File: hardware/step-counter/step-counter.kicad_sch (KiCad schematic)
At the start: 50 parts, among them J1 Conn_01x10_Male, J2 Conn_01x14_Male, J3 Conn_01x10_Male, J4 Conn_Power, U1 74HC161, U10 74HC161, U11 74LVC1G02, U12 74LVC2G04, U13 74HC4024, U14 74LVC1G332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

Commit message: Updated PCBs
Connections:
- net Q0: now also J2.13 (Pin_13); no longer J2.8 (Pin_8)
- net Q1: now also J2.12 (Pin_12); no longer J2.9 (Pin_9)
- net Q2: now also J2.11 (Pin_11); no longer J2.10 (Pin_10)
- net Q3: now also J2.10 (Pin_10); no longer J2.11 (Pin_11)
- net Q4: now also J2.9 (Pin_9); no longer J2.12 (Pin_12)
- net Q5: now also J2.8 (Pin_8); no longer J2.13 (Pin_13)
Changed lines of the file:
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@@
     (effects (font (size 1.27 1.27)) (justify left bottom))
   )
-  (label "Q1" (at 393.7 153.67 0)
+  (label "Q1" (at 393.7 161.29 0)
     (effects (font (size 1.27 1.27)) (justify left bottom))
   )
@@
     (effects (font (size 1.27 1.27)) (justify right bottom))
   )
-  (label "Q0" (at 393.7 151.13 0)
+  (label "Q0" (at 393.7 163.83 0)
     (effects (font (size 1.27 1.27)) (justify left bottom))
   )
-  (label "Q3" (at 393.7 158.75 0)
+  (label "Q3" (at 393.7 156.21 0)
     (effects (font (size 1.27 1.27)) (justify left bottom))
   )
@@
     (effects (font (size 1.27 1.27)) (justify right bottom))
   )
-  (label "Q5" (at 393.7 163.83 0)
+  (label "Q5" (at 393.7 151.13 0)
     (effects (font (size 1.27 1.27)) (justify left bottom))
   )
-  (label "Q2" (at 393.7 156.21 0)
+  (label "Q2" (at 393.7 158.75 0)
     (effects (font (size 1.27 1.27)) (justify left bottom))
   )
@@
     (effects (font (size 1.27 1.27)) (justify left bottom))
   )
-  (label "Q4" (at 393.7 161.29 0)
+  (label "Q4" (at 393.7 153.67 0)
     (effects (font (size 1.27 1.27)) (justify left bottom))
   )

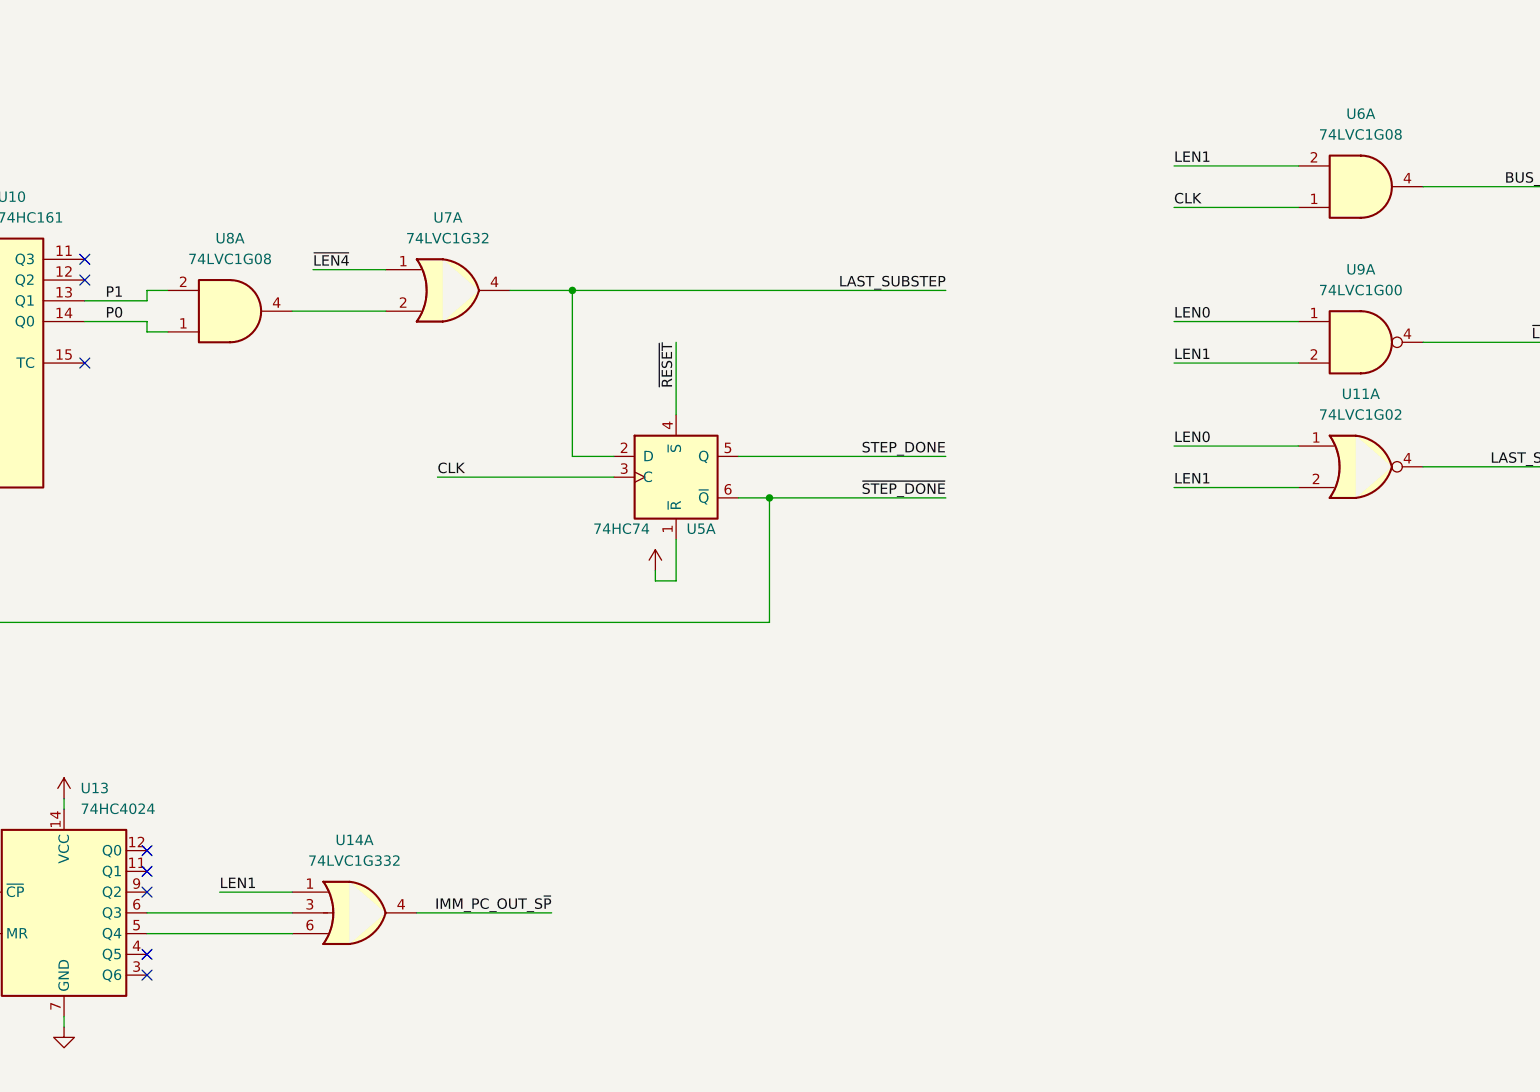
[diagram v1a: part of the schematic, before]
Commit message: Updated opcode and step counter PCBs
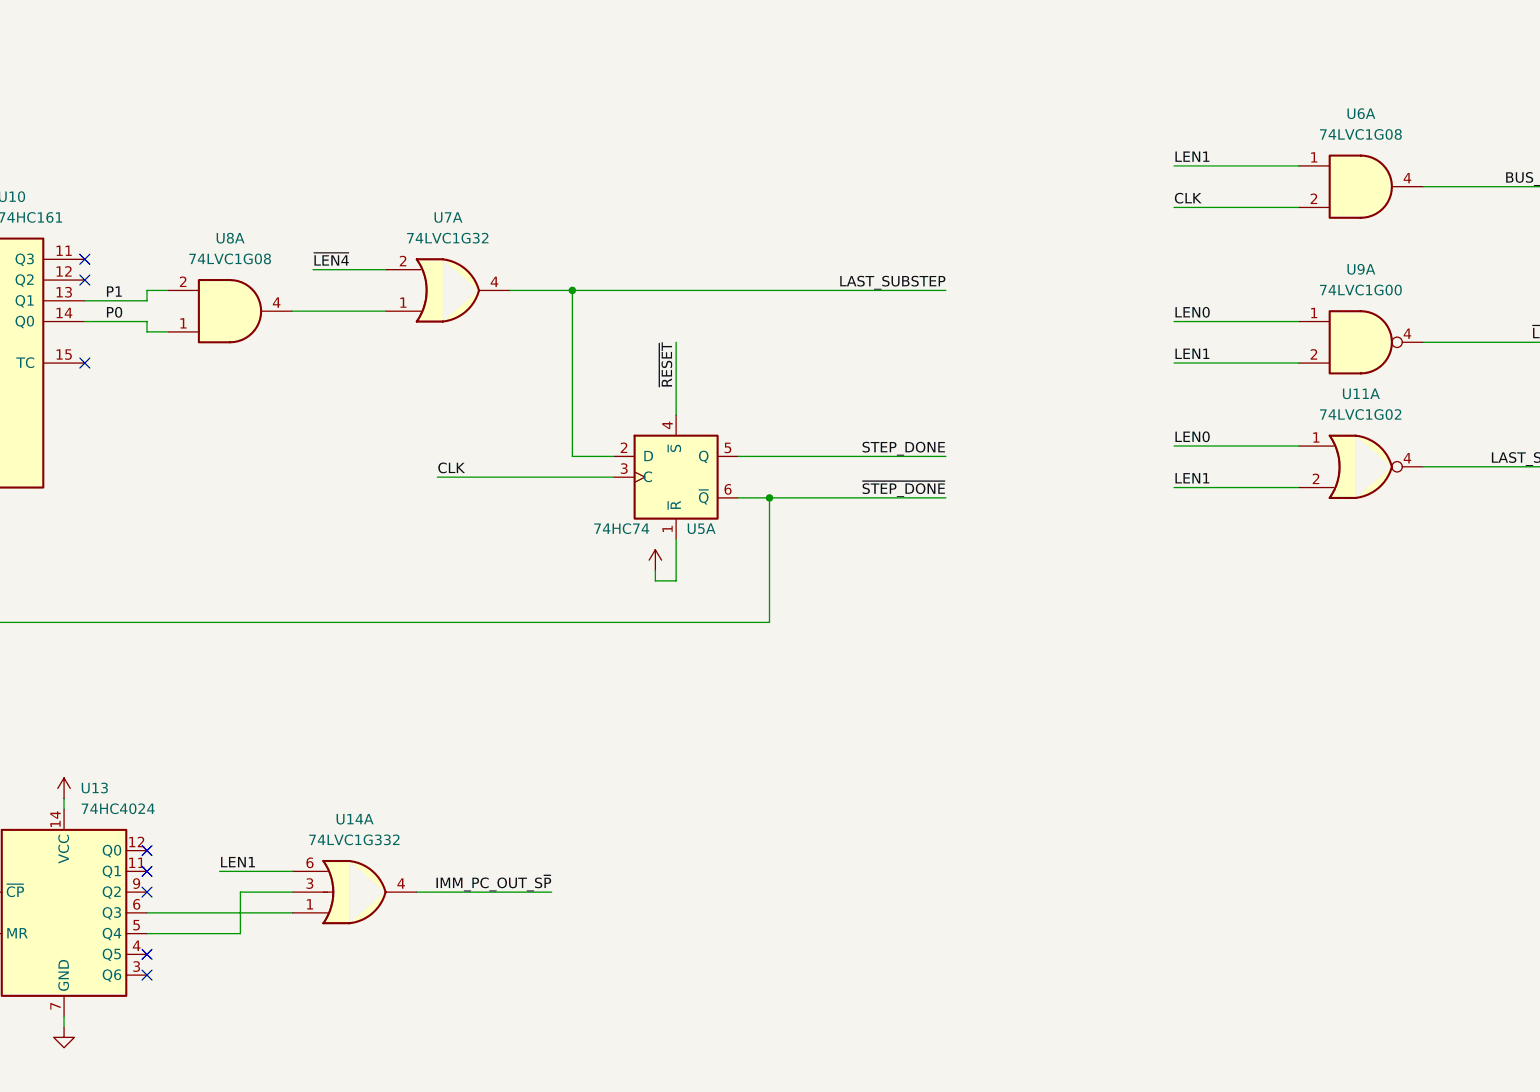
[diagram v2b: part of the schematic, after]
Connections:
- net CLK: now also U6.2; no longer U6.1
- net LEN1: now also U14.6, U6.1; no longer U14.1, U6.2
- net ~{LEN4}: now also U7.2; no longer U7.1
- net at U13.5 (Q4): now also U14.3; no longer U14.6
- net at U13.6 (Q3): now also U14.1; no longer U14.3
- net at U8.4: now also U7.1; no longer U7.2
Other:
- moved on the sheet: U14A
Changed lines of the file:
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@@
+    (stroke (width 0) (type default) (color 0 0 0 0))
+  )
+  (wire (pts (xy 96.52 246.38) (xy 114.3 246.38))
     (stroke (width 0) (type default) (color 0 0 0 0))
   )
@@
     (stroke (width 0) (type default) (color 0 0 0 0))
   )
-  (wire (pts (xy 96.52 246.38) (xy 114.3 246.38))
-    (stroke (width 0) (type default) (color 0 0 0 0))
-  )
   (wire (pts (xy 140.97 97.79) (xy 144.78 97.79))
     (stroke (width 0) (type default) (color 0 0 0 0))
@@
     (stroke (width 0) (type default) (color 0 0 0 0))
   )
-  (wire (pts (xy 129.54 246.38) (xy 146.05 246.38))
+  (wire (pts (xy 129.54 243.84) (xy 146.05 243.84))
     (stroke (width 0) (type default) (color 0 0 0 0))
   )
@@
     (stroke (width 0) (type default) (color 0 0 0 0))
   )
-  (wire (pts (xy 105.41 243.84) (xy 114.3 243.84))
+  (wire (pts (xy 105.41 241.3) (xy 114.3 241.3))
     (stroke (width 0) (type default) (color 0 0 0 0))
   )
@@
     (stroke (width 0) (type default) (color 0 0 0 0))
   )
+  (wire (pts (xy 107.95 243.84) (xy 114.3 243.84))
+    (stroke (width 0) (type default) (color 0 0 0 0))
+  )
   (wire (pts (xy 66.04 309.88) (xy 76.2 309.88))
     (stroke (width 0) (type default) (color 0 0 0 0))
@@
     (stroke (width 0) (type default) (color 0 0 0 0))
   )
+  (wire (pts (xy 107.95 248.92) (xy 107.95 243.84))
+    (stroke (width 0) (type default) (color 0 0 0 0))
+  )
   (wire (pts (xy 140.97 87.63) (xy 156.21 87.63))
     (stroke (width 0) (type default) (color 0 0 0 0))
@@
     (stroke (width 0) (type default) (color 0 0 0 0))
   )
-  (wire (pts (xy 96.52 248.92) (xy 114.3 248.92))
-    (stroke (width 0) (type default) (color 0 0 0 0))
-  )
   (wire (pts (xy 55.88 179.07) (xy 55.88 210.82))
+    (stroke (width 0) (type default) (color 0 0 0 0))
+  )
+  (wire (pts (xy 96.52 248.92) (xy 107.95 248.92))
     (stroke (width 0) (type default) (color 0 0 0 0))
   )
@@
     (effects (font (size 1.27 1.27)) (justify left bottom))
   )
-  (label "IMM_PC_OUT_S~{P}" (at 146.05 246.38 180)
+  (label "IMM_PC_OUT_S~{P}" (at 146.05 243.84 180)
     (effects (font (size 1.27 1.27)) (justify right bottom))
   )
@@
     (effects (font (size 1.27 1.27)) (justify left bottom))
   )
-  (label "LEN1" (at 105.41 243.84 0)
+  (label "LEN1" (at 105.41 241.3 0)
     (effects (font (size 1.27 1.27)) (justify left bottom))
   )
@@
     (pin "4")
   )
-  (symbol (lib_id "riscv-serial:74LVC1G332") (at 121.92 246.38 0) (unit 1)
-    (in_bom yes) (on_board yes) (fields_autoplaced)
-    (property "Reference" "U14" (id 0) (at 121.92 237.49 0))
-    (property "Value" "74LVC1G332" (id 1) (at 121.92 240.03 0))
-    (property "Footprint" "Package_TO_SOT_SMD:SOT-23-6_Handsoldering" (id 2) (at 121.158 247.142 0)
-      (effects (font (size 1.27 1.27)) hide)
-    )
-    (property "Datasheet" "" (id 3) (at 121.158 247.142 0)
+  (symbol (lib_id "riscv-serial:74LVC1G332") (at 121.92 243.84 0) (mirror x) (unit 1)
+    (in_bom yes) (on_board yes) (fields_autoplaced)
+    (property "Reference" "U14" (id 0) (at 121.92 234.95 0))
+    (property "Value" "74LVC1G332" (id 1) (at 121.92 237.49 0))
+    (property "Footprint" "Package_TO_SOT_SMD:SOT-23-6_Handsoldering" (id 2) (at 121.158 243.078 0)
+      (effects (font (size 1.27 1.27)) hide)
+    )
+    (property "Datasheet" "" (id 3) (at 121.158 243.078 0)
       (effects (font (size 1.27 1.27)) hide)
     )
@@
     (pin "1")
   )
-  (symbol (lib_id "riscv-serial:74LVC1G08") (at 245.11 157.48 0) (mirror x) (unit 1)
+  (symbol (lib_id "riscv-serial:74LVC1G08") (at 245.11 157.48 0) (unit 1)
     (in_bom yes) (on_board yes) (fields_autoplaced)
     (property "Reference" "U6" (id 0) (at 245.11 148.59 0))
     (property "Value" "74LVC1G08" (id 1) (at 245.11 151.13 0))
-    (property "Footprint" "Package_TO_SOT_SMD:SOT-23-5_HandSoldering" (id 2) (at 245.11 158.75 0)
-      (effects (font (size 1.27 1.27)) hide)
-    )
-    (property "Datasheet" "" (id 3) (at 245.11 158.75 0)
+    (property "Footprint" "Package_TO_SOT_SMD:SOT-23-5_HandSoldering" (id 2) (at 245.11 156.21 0)
+      (effects (font (size 1.27 1.27)) hide)
+    )
+    (property "Datasheet" "" (id 3) (at 245.11 156.21 0)
       (effects (font (size 1.27 1.27)) hide)
     )
@@
     (pin "4")
   )
-  (symbol (lib_id "riscv-serial:74LVC1G32") (at 133.35 170.18 0) (unit 1)
+  (symbol (lib_id "riscv-serial:74LVC1G32") (at 133.35 170.18 0) (mirror x) (unit 1)
     (in_bom yes) (on_board yes) (fields_autoplaced)
     (property "Reference" "U7" (id 0) (at 133.35 161.29 0))
     (property "Value" "74LVC1G32" (id 1) (at 133.35 163.83 0))
-    (property "Footprint" "Package_TO_SOT_SMD:SOT-23-5_HandSoldering" (id 2) (at 132.588 170.942 0)
-      (effects (font (size 1.27 1.27)) hide)
-    )
-    (property "Datasheet" "" (id 3) (at 132.588 170.942 0)
-      (effects (font (size 1.27 1.27)) hide)
-    )
+    (property "Footprint" "Package_TO_SOT_SMD:SOT-23-5_HandSoldering" (id 2) (at 132.588 169.418 0)
+      (effects (font (size 1.27 1.27)) hide)
+    )
+    (property "Datasheet" "" (id 3) (at 132.588 169.418 0)
+      (effects (font (size 1.27 1.27)) hide)
+    )
